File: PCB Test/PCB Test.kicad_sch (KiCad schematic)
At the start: 39 parts, among them J1 Screw_Terminal_01x02, J5 Screw_Terminal_01x02, J6 Conn_02x03_Odd_Even, Q2 NMOS, Q3 NMOS, SW1 SW_Push, U1 ATmega4808-A, U2 TCRT5000, U3 TCRT5000, U4 TCRT5000, U5 MCP1700x-330xxTO

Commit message: Added bulk capacitor, couldn't figure out how to add 2x5 header. Asking AI for general feedback
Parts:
- added BT1, BT2, BT3, BT4: Battery_Cell, symbol Device:Battery_Cell
- added C1, C2: C, symbol Device:C
- J1: value Screw_Terminal_01x02 -> Motor Terminal 2
- J5: value Screw_Terminal_01x02 -> Motor Terminal 1
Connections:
- net +4.8V: now also BT1.1 (+)
- net GND: now also BT4.2 (-), C1.1, C2.1
- net VDD: now also C1.2, C2.2
- new net: BT1.2 (-), BT2.1 (+)
- new net: BT2.2 (-), BT3.1 (+)
- new net: BT3.2 (-), BT4.1 (+)
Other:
- note added: "Battery and Voltage Regulation"
- note removed: "Voltage Regulation and Decoupling"
- moved on the sheet: J6

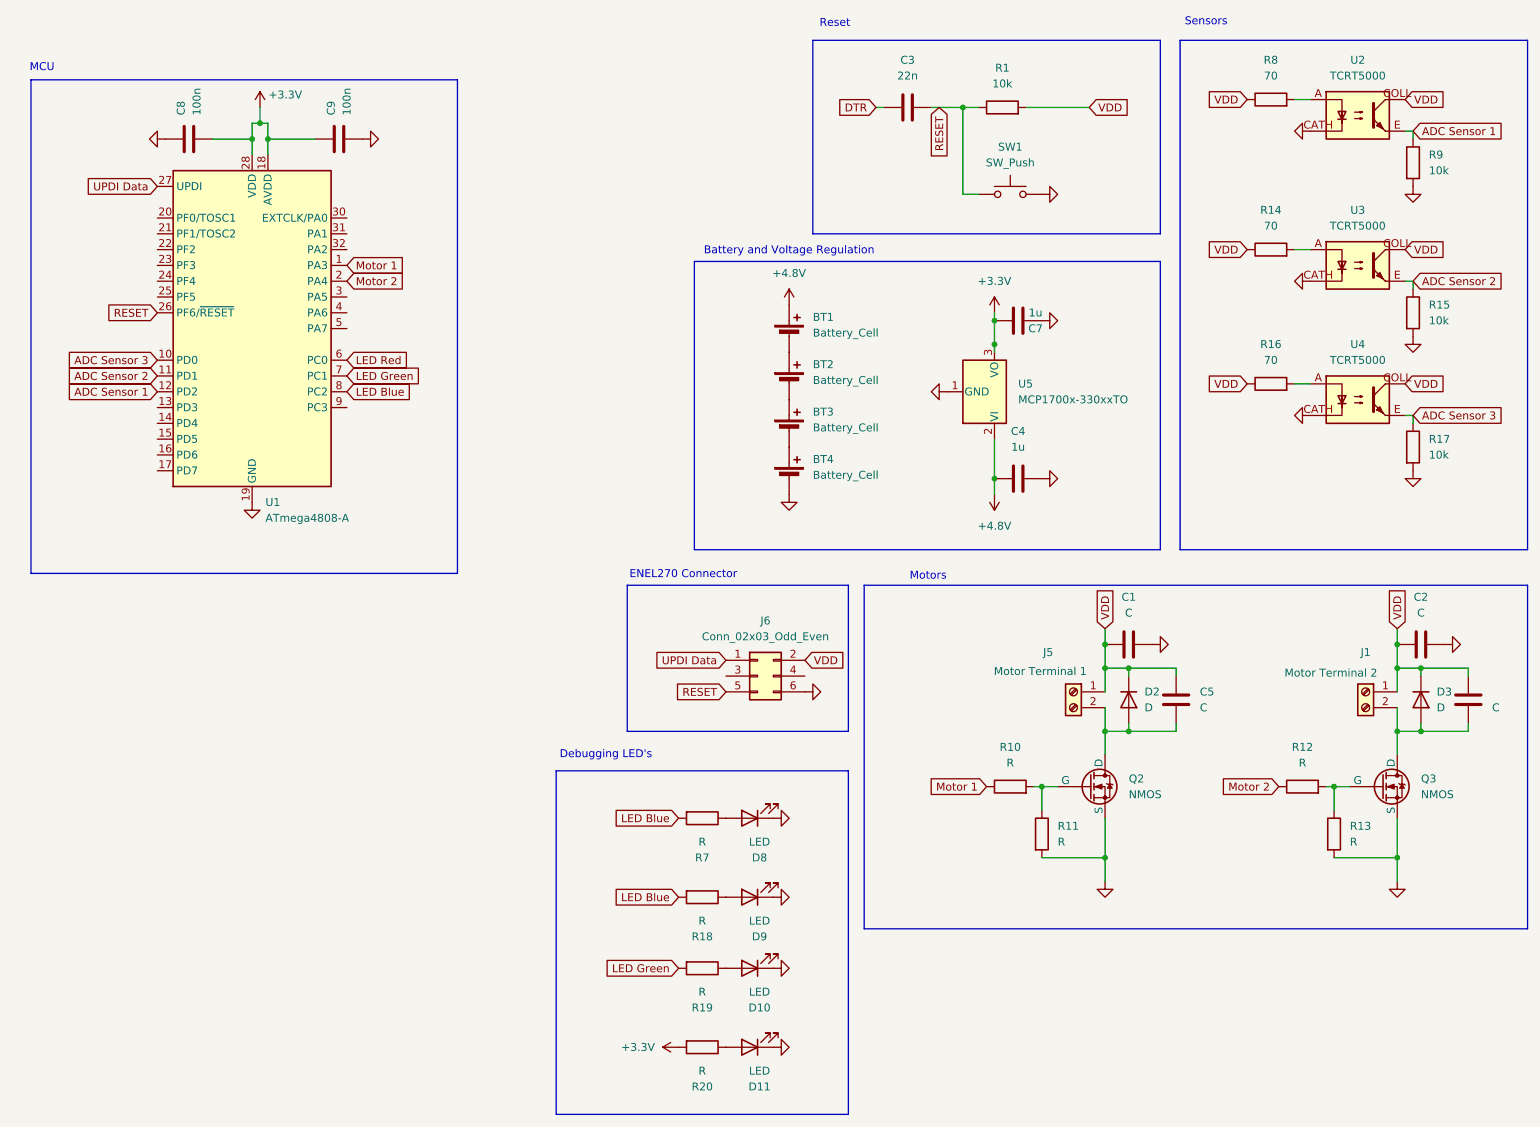
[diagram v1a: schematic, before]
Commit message: Added resistor and capacitor values, almost ready to move on to the schematic
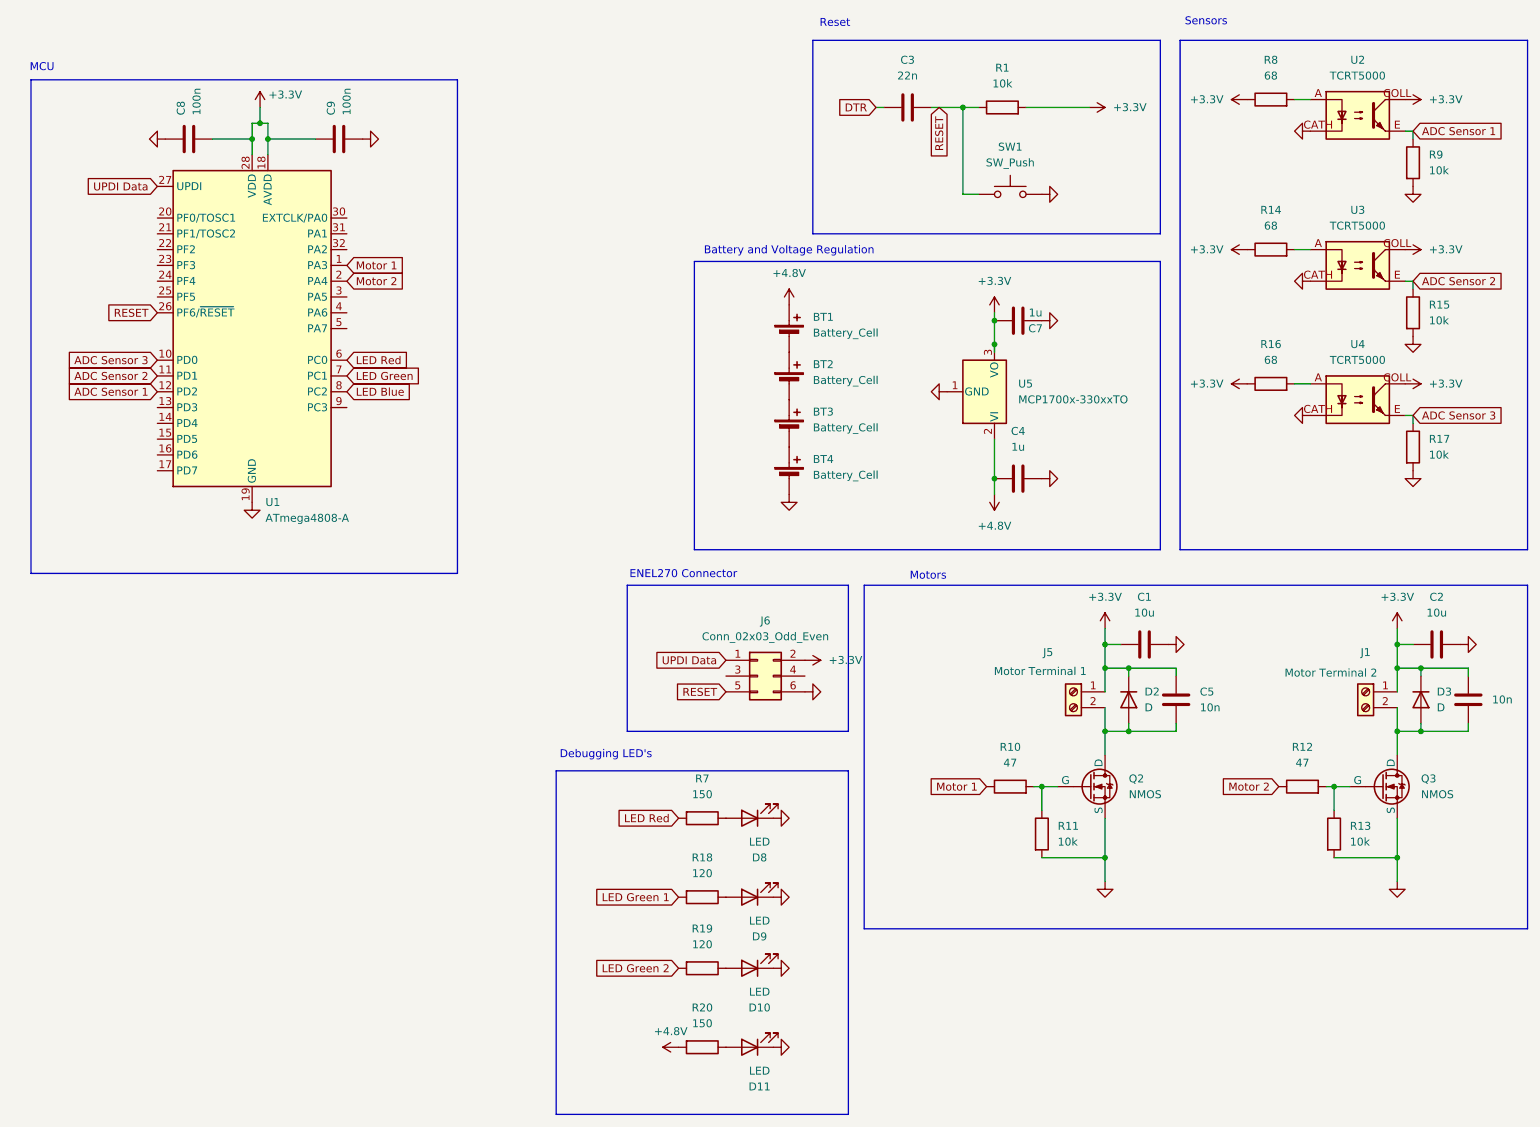
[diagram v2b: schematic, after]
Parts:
- C1, C2: value C -> 10u
- C5, C6: value C -> 10n
- R10, R12: value R -> 47
- R11, R13: value R -> 10k
- R14, R16, R8: value 70 -> 68
- R18, R19: value R -> 120
- R20, R7: value R -> 150
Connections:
- net VDD is gone; now on net +3.3V: C1.2, C2.2, C5.1, C6.1, D2.1 (K), D3.1 (K), J1.1 (Pin_1), J5.1 (Pin_1), J6.2 (Pin_2), R1.2, R14.1, R16.1, R8.1, U2.COLL, U3.COLL, U4.COLL
- net +3.3V: no longer R20.2
- net +4.8V: now also R20.2
- net LED Blue: no longer R18.2, R7.2
- net LED Green: no longer R19.2
- net LED Red: now also R7.2
- new net LED Green 1: R18.2
- new net LED Green 2: R19.2
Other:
- moved on the sheet: C1, C2

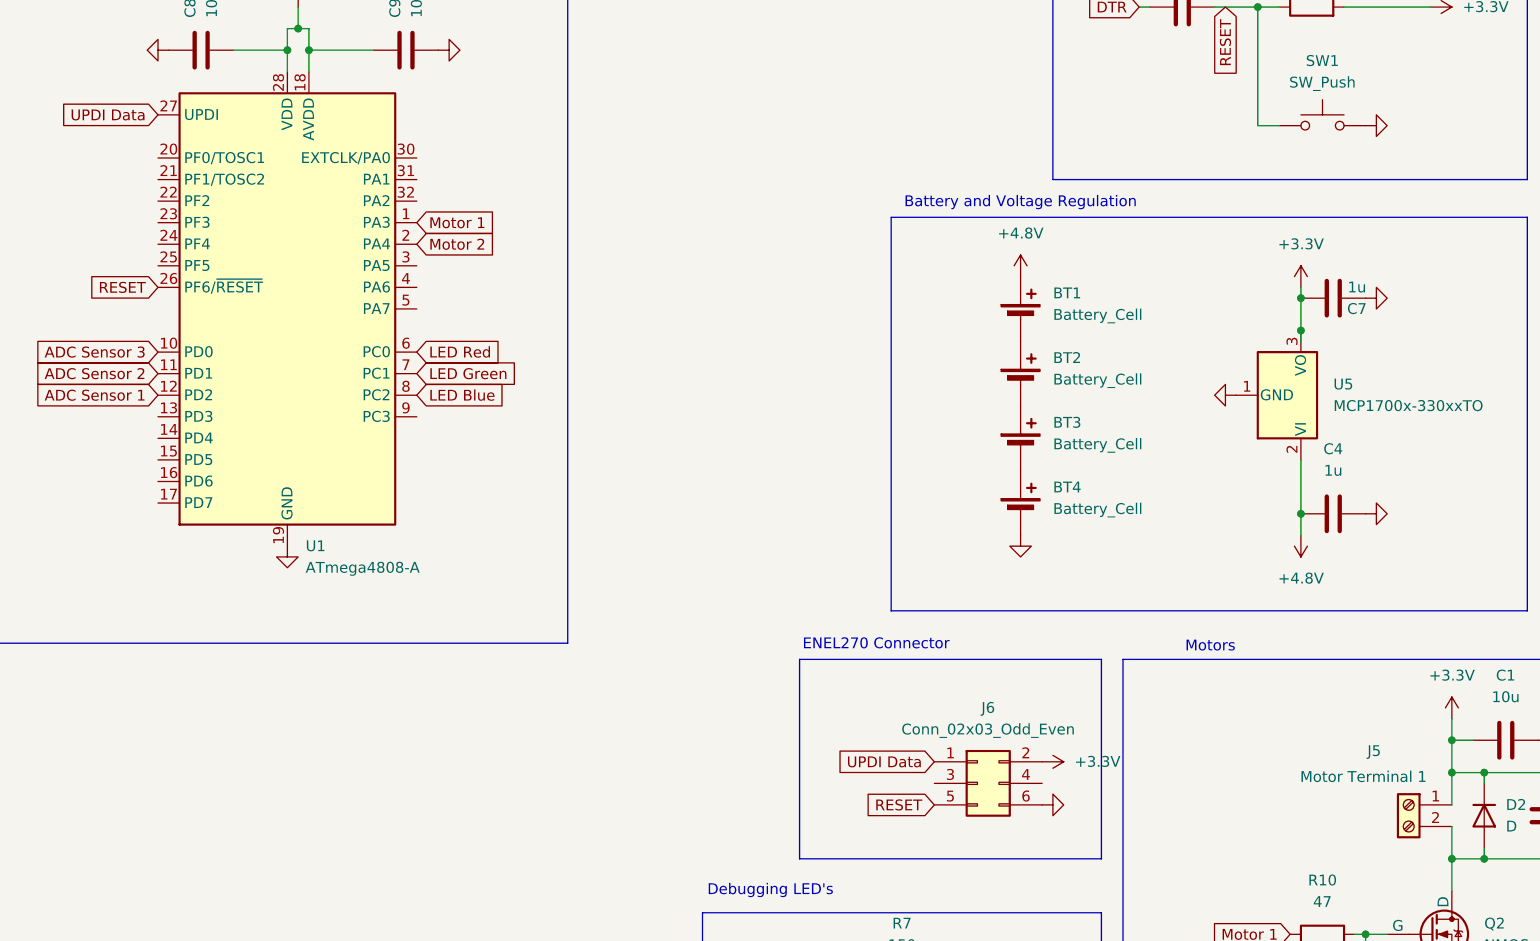
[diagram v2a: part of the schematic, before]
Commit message: Ran ERC, fixed all the warning, ready to move on to PCB layout
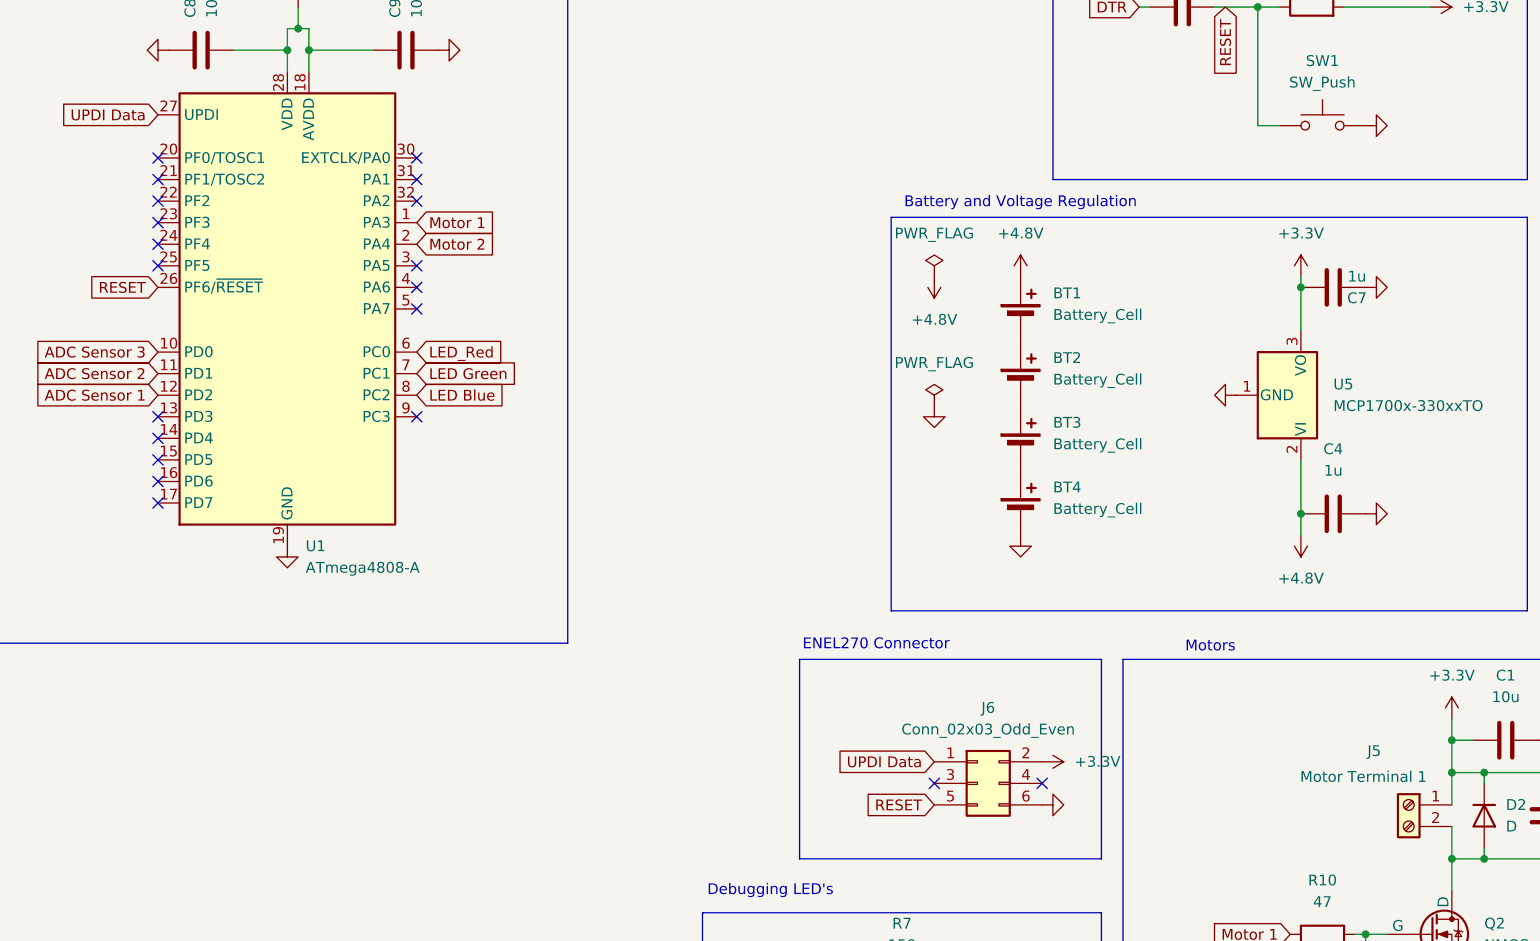
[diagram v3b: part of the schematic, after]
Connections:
- net LED Red: no longer U1.6 (PC0)
- new net LED_Red: U1.6 (PC0)
- no-connect marks 0 -> 20
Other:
- moved on the sheet: C7

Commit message: Assigned footprints to all components
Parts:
- removed BT2, BT3: Battery_Cell, symbol Device:Battery_Cell
- added R21, R22: 330, Resistor_SMD:R_0805_2012Metric_Pad1.20x1.40mm_HandSolder, symbol Device:R
- added SW2, SW3: SW_Push, Button_Switch_THT:SW_PUSH_1P1T_6x3.5mm_H4.3_APEM_MJTP1243, symbol Switch:SW_Push
- BT1: footprint (none) -> Battery:BatteryHolder_Keystone_2462_2xAA
- BT2: renamed from BT4; footprint (none) -> Battery:BatteryHolder_Keystone_2462_2xAA
- C1, C2, C4, C7: footprint (none) -> Capacitor_THT:C_Radial_D6.3mm_H5.0mm_P2.50mm
- C3, C5, C6, C8, C9: footprint (none) -> Capacitor_SMD:C_0805_2012Metric_Pad1.18x1.45mm_HandSolder
- D10, D11, D8, D9: footprint (none) -> LED_THT:LED_D5.0mm
- D2, D3: footprint (none) -> FBY8:P30_D7.3x22
- J1, J5: footprint (none) -> TerminalBlock:TerminalBlock_MaiXu_MX126-5.0-02P_1x02_P5.00mm
- J6: footprint (none) -> Connector:Tag-Connect_TC2030-IDC-FP_2x03_P1.27mm_Vertical
- Q2, Q3: footprint (none) -> Package_TO_SOT_SMD:SC-59_Handsoldering
- R1, R10, R11, R12, R13, R14, R15, R16, R17, R18, R19, R20, R7, R8, R9: footprint (none) -> Resistor_SMD:R_0805_2012Metric_Pad1.20x1.40mm_HandSolder
- SW1: footprint (none) -> Button_Switch_THT:SW_PUSH_1P1T_6x3.5mm_H4.3_APEM_MJTP1243
- U2, U3, U4: footprint tcrt5000:tcrt5000 -> OptoDevice:Vishay_TCRT5000
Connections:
- net GND: now also R21.2, R22.2
- net at BT1.2 (-): now also BT2.1 (+)
- net Button 1: now reaches U1.3 (PA5)
- net Button 1: now also SW2.1
- net Button 2: now reaches U1.4 (PA6)
- net Button 2: now also SW3.1
- new net: R22.1, SW3.2
- new net: R21.1, SW2.2
- no-connect marks 20 -> 18
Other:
- note added: "LED's and Buttons"
- note removed: "Debugging LED's"
- moved on the sheet: BT2
